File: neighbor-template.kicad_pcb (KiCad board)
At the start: 4 copper layers, 70.7 x 53.3 mm, 7 parts, among them J1 NEIGHBOR1, J2 NEIGHBOR2, J7 BONUS_ROW

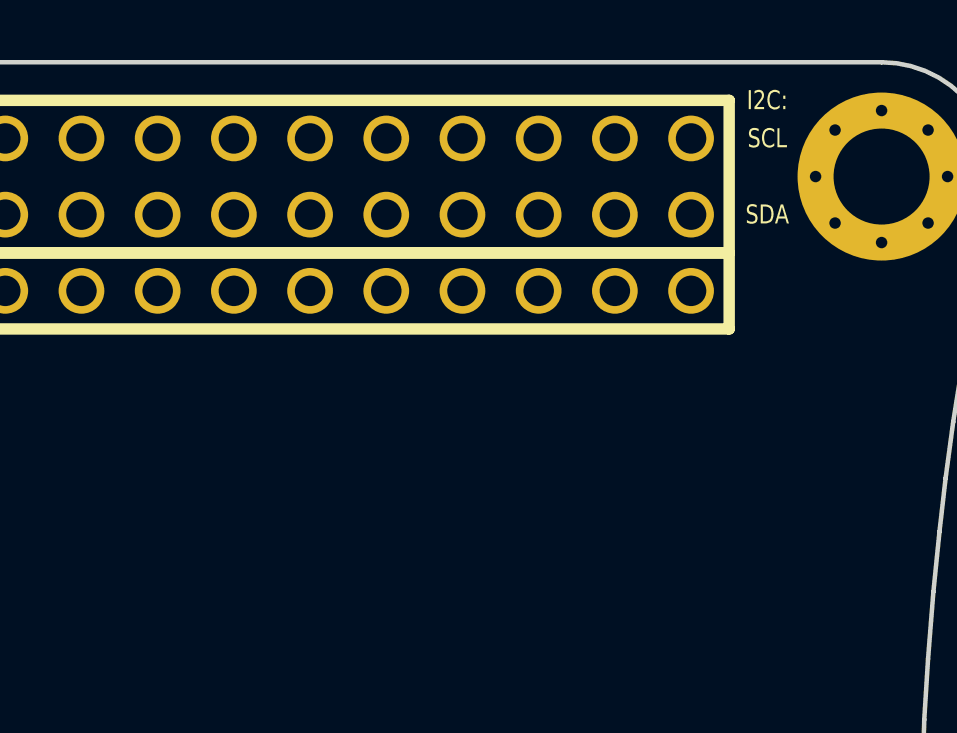
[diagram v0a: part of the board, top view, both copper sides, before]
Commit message: add identification EEPROM to layout
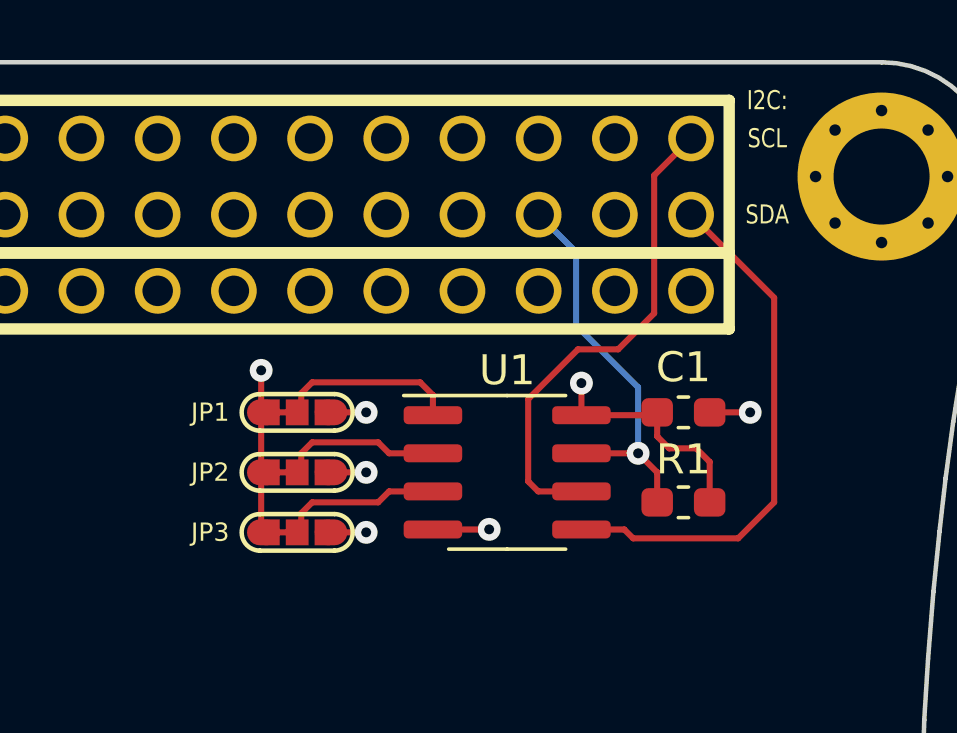
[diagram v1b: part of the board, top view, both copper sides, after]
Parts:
- added C1: 100nF, Capacitor_SMD:C_0603_1608Metric_Pad1.05x0.95mm_HandSolder, F.Cu at (169.9, 80.2)
- added JP1: Jumper_3_Bridged12, neighbor:0603-JUMPER-3-BRIDGED12, F.Cu at (157.1, 80.2)
- added JP2: Jumper_3_Bridged12, neighbor:0603-JUMPER-3-BRIDGED12, F.Cu at (157.1, 82.2)
- added JP3: Jumper_3_Bridged12, neighbor:0603-JUMPER-3-BRIDGED12, F.Cu at (157.1, 84.2)
- added R1: 10k, Resistor_SMD:R_0603_1608Metric_Pad1.05x0.95mm_HandSolder, F.Cu at (169.9, 83.2)
- added U1: M24C02-FMN6TP, Package_SO:SOIC-8_3.9x4.9mm_P1.27mm, F.Cu at (164.1, 82.2)
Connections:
- J1 pad 10: (no net) -> /P1_1
- J1 pad 11: (no net) -> /CLK0
- J1 pad 12: (no net) -> /P1_2
- J1 pad 13: (no net) -> /P1_5
- J1 pad 14: (no net) -> /P5_2
- J1 pad 15: (no net) -> /P1_7
- J1 pad 16: (no net) -> /P1_6
- J1 pad 17: (no net) -> /P1_9
- J1 pad 18: (no net) -> /P1_8
- J1 pad 19: (no net) -> /P5_3
- J1 pad 20: (no net) -> /P1_10
- J1 pad 21: (no net) -> /P1_12
- J1 pad 22: (no net) -> /P1_11
- J1 pad 23: (no net) -> /P5_5
- J1 pad 24: (no net) -> /P5_4
- J1 pad 25: (no net) -> /P1_14
- J1 pad 26: (no net) -> /P1_13
- J1 pad 27: (no net) -> /P5_6
- J1 pad 28: (no net) -> /P1_15
- J1 pad 29: (no net) -> /P5_7
- J1 pad 3: (no net) -> /P4_9
- J1 pad 30: (no net) -> /P1_16
- J1 pad 31: (no net) -> /P1_18
- J1 pad 32: (no net) -> /P1_17
- J1 pad 33: (no net) -> /P9_5
- J1 pad 34: (no net) -> /P9_6
- J1 pad 35: (no net) -> /P2_0
- J1 pad 36: (no net) -> /P6_0
- J1 pad 37: (no net) -> /P1_20
- J1 pad 38: (no net) -> /P1_19
- J1 pad 39: (no net) -> /P1_4
- J1 pad 4: (no net) -> /P0_0
- J1 pad 40: (no net) -> /P1_3
- J1 pad 5: (no net) -> /P4_10
- J1 pad 6: (no net) -> /P0_1
- J1 pad 7: (no net) -> /P1_0
- J1 pad 8: (no net) -> /P5_0
- J1 pad 9: (no net) -> /P5_1
- J2 pad 10: (no net) -> /P4_6
- J2 pad 11: (no net) -> /P4_7
- J2 pad 12: (no net) -> /CLK2
- J2 pad 13: (no net) -> /P2_8
- J2 pad 14: (no net) -> /P2_7
- J2 pad 15: (no net) -> /P2_6
- J2 pad 16: (no net) -> /P7_7
- J2 pad 17: (no net) -> /WAKEUP0
- J2 pad 18: (no net) -> /P2_5
- J2 pad 19: (no net) -> /P2_4
- J2 pad 20: (no net) -> /P2_3
- J2 pad 21: (no net) -> /PF_4
- J2 pad 22: (no net) -> /P3_2
- J2 pad 23: (no net) -> /P7_2
- J2 pad 24: (no net) -> /P3_1
- J2 pad 25: (no net) -> /P7_1
- J2 pad 26: (no net) -> /P3_0
- J2 pad 27: (no net) -> /P7_0
- J2 pad 28: (no net) -> /P3_4
- J2 pad 29: (no net) -> /P6_8
- J2 pad 3: (no net) -> /P4_8
- J2 pad 30: (no net) -> /P3_7
- J2 pad 31: (no net) -> /P6_7
- J2 pad 32: (no net) -> /P3_3
- J2 pad 33: (no net) -> /P2_2
- J2 pad 34: (no net) -> /P6_6
- J2 pad 35: (no net) -> /P2_1
- J2 pad 36: (no net) -> /P6_3
- J2 pad 37: (no net) -> /P3_5
- J2 pad 38: (no net) -> /P3_6
- J2 pad 39: (no net) -> /I2C0_SDA
- J2 pad 4: (no net) -> /P4_0
- J2 pad 40: (no net) -> /I2C0_SCL
- J2 pad 5: (no net) -> /ADC0_0
- J2 pad 6: (no net) -> /P4_5
- J2 pad 7: (no net) -> /P4_4
- J2 pad 8: (no net) -> /P4_2
- J2 pad 9: (no net) -> /P4_3
- J7 pad 11: (no net) -> /RESET
- J7 pad 12: (no net) -> /VBAT
- J7 pad 13: (no net) -> /P2_11
- J7 pad 14: (no net) -> /P2_10
- J7 pad 15: (no net) -> /P6_10
- J7 pad 16: (no net) -> /P6_9
- J7 pad 17: (no net) -> /P6_2
- J7 pad 18: (no net) -> /P6_1
- J7 pad 2: (no net) -> /P6_4
- J7 pad 3: (no net) -> /P6_5
- J7 pad 4: (no net) -> /ADC0_5
- J7 pad 5: (no net) -> /ADC0_2
- J7 pad 6: (no net) -> /P2_9
- J7 pad 7: (no net) -> /P2_12
- J7 pad 8: (no net) -> /P2_13
- J7 pad 9: (no net) -> /RTC_ALARM
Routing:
- net /I2C0_SDA: track 0.00 -> 17.8 mm
- net /I2C0_SCL: track 0.00 -> 16.4 mm
- net /P2_1: track 0.00 -> 13.1 mm, vias 0 -> 1
- net VCC: track 0.00 -> 11.4 mm, vias 0 -> 4
- net GND: track 0.00 -> 8.65 mm, vias 0 -> 3
- net /E0: track 0.00 -> 6.02 mm
- net /E2: track 0.00 -> 5.33 mm
- net /E1: track 0.00 -> 5.33 mm

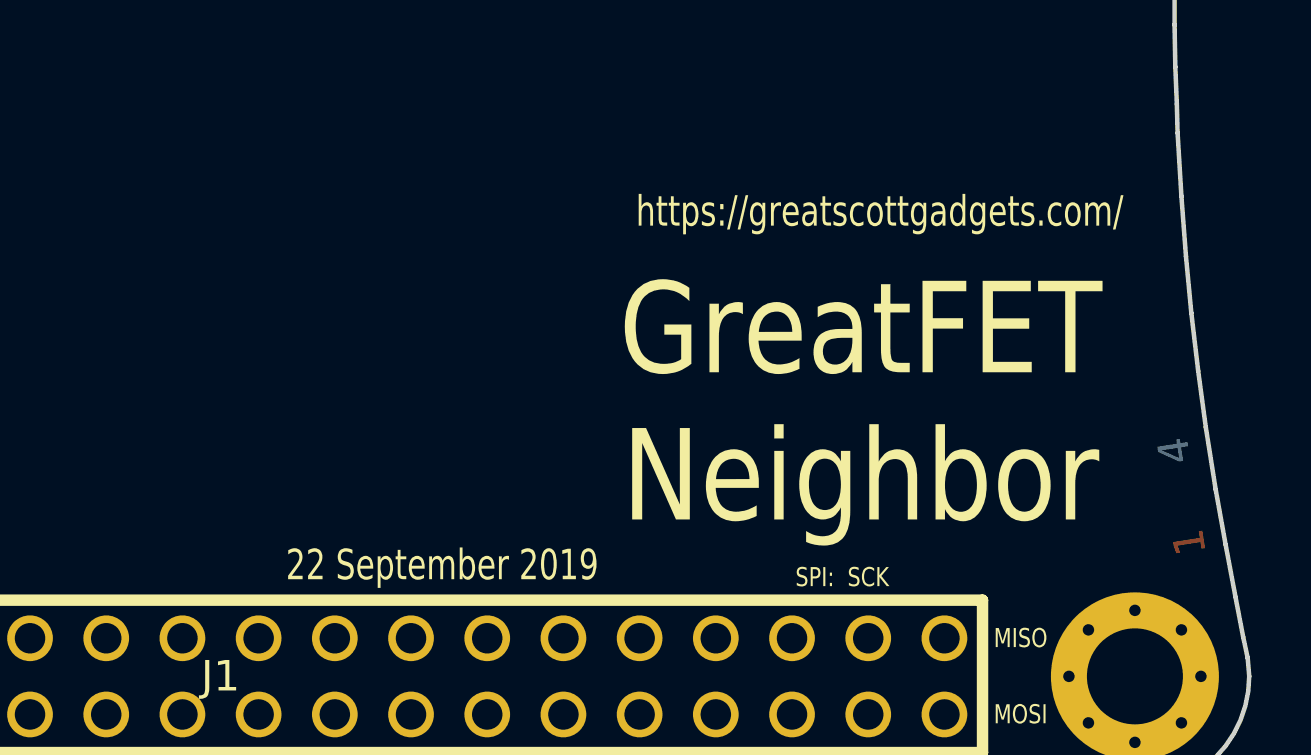
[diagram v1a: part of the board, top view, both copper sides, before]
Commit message: remove Great Scott Gadgets branding
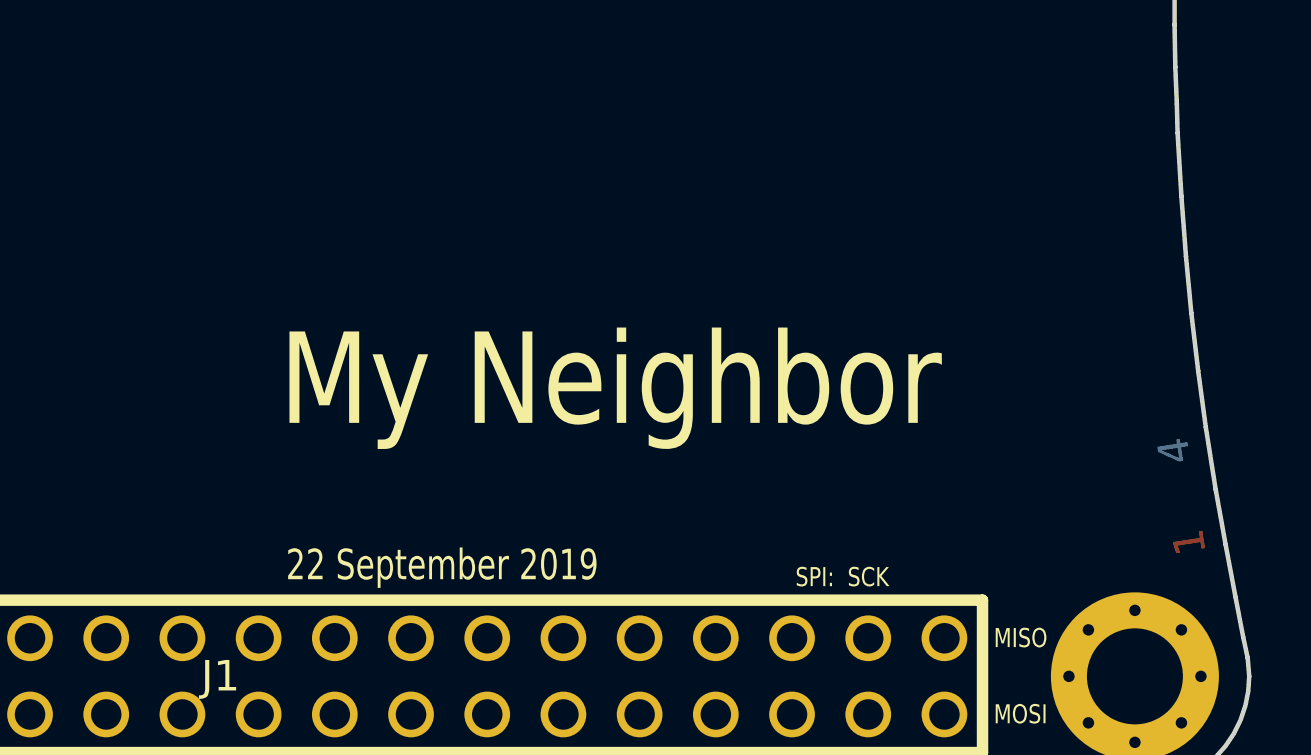
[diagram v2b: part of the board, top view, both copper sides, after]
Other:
- board text added: "My Neighbor"
- board text removed: "GreatFET Neighbor"
- board text removed: "https://greatscottgadgets.com/"
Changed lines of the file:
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@@
   (general
     (thickness 1.6)
-    (drawings 122)
+    (drawings 121)
     (tracks 64)
     (zones 0)
@@
     (effects (font (size 1.016 1.016) (thickness 0.1778)))
   )
-  (gr_text https://greatscottgadgets.com/ (at 168.021 102.616) (layer F.SilkS)
-    (effects (font (size 1.016 0.762) (thickness 0.1524)))
-  )
   (gr_text GND (at 118.999 73.406) (layer F.SilkS)
     (effects (font (size 0.635 0.508) (thickness 0.1016)))
@@
   (gr_arc (start 176.53 118.11) (end 180.34 118.11) (angle 90) (layer Edge.Cuts) (width 0.15))
   (gr_arc (start 279.4508 95.25) (end 177.8508 95.25) (angle 12.5) (layer Cmts.User) (width 0.15))
-  (gr_text "GreatFET\nNeighbor" (at 167.386 109.0168) (layer F.SilkS)
+  (gr_text "My Neighbor" (at 159.05 108.25) (layer F.SilkS)
     (effects (font (size 3.048 2.54) (thickness 0.4572)))
   )
@@
   (segment (start 168.95 76.95) (end 167.75 78.15) (width 0.2032) (layer F.Cu) (net 79))
   (segment (start 166.410198 78.15) (end 164.75 79.810198) (width 0.2032) (layer F.Cu) (net 79))
+  (segment (start 161.575 80.345) (end 161.575 79.675) (width 0.2032) (layer F.Cu) (net 96))
+  (segment (start 161.575 79.675) (end 161.15 79.25) (width 0.2032) (layer F.Cu) (net 96))
+  (segment (start 161.15 79.25) (end 157.55 79.25) (width 0.2032) (layer F.Cu) (net 96))
+  (segment (start 157.185001 79.945199) (end 157.185001 80.25) (width 0.2032) (layer F.Cu) (net 96))
+  (segment (start 157.55 79.25) (end 157.185001 79.614999) (width 0.2032) (layer F.Cu) (net 96))
+  (segment (start 157.185001 79.614999) (end 157.185001 79.945199) (width 0.2032) (layer F.Cu) (net 96))
+  (segment (start 161.575 81.615) (end 160.115 81.615) (width 0.2032) (layer F.Cu) (net 97))
+  (segment (start 160.115 81.615) (end 159.75 81.25) (width 0.2032) (layer F.Cu) (net 97))
+  (segment (start 159.75 81.25) (end 157.55 81.25) (width 0.2032) (layer F.Cu) (net 97))
+  (segment (start 157.185001 81.945199) (end 157.185001 82.25) (width 0.2032) (layer F.Cu) (net 97))
+  (segment (start 157.55 81.25) (end 157.185001 81.614999) (width 0.2032) (layer F.Cu) (net 97))
+  (segment (start 157.185001 81.614999) (end 157.185001 81.945199) (width 0.2032) (layer F.Cu) (net 97))
   (segment (start 161.575 82.885) (end 160.115 82.885) (width 0.2032) (layer F.Cu) (net 98))
   (segment (start 160.115 82.885) (end 159.75 83.25) (width 0.2032) (layer F.Cu) (net 98))
@@
   (segment (start 157.55 83.25) (end 157.185001 83.614999) (width 0.2032) (layer F.Cu) (net 98))
   (segment (start 157.185001 83.614999) (end 157.185001 83.945199) (width 0.2032) (layer F.Cu) (net 98))
-  (segment (start 161.575 81.615) (end 160.115 81.615) (width 0.2032) (layer F.Cu) (net 97))
-  (segment (start 160.115 81.615) (end 159.75 81.25) (width 0.2032) (layer F.Cu) (net 97))
-  (segment (start 159.75 81.25) (end 157.55 81.25) (width 0.2032) (layer F.Cu) (net 97))
-  (segment (start 157.185001 81.945199) (end 157.185001 82.25) (width 0.2032) (layer F.Cu) (net 97))
-  (segment (start 157.55 81.25) (end 157.185001 81.614999) (width 0.2032) (layer F.Cu) (net 97))
-  (segment (start 157.185001 81.614999) (end 157.185001 81.945199) (width 0.2032) (layer F.Cu) (net 97))
-  (segment (start 161.575 80.345) (end 161.575 79.675) (width 0.2032) (layer F.Cu) (net 96))
-  (segment (start 161.575 79.675) (end 161.15 79.25) (width 0.2032) (layer F.Cu) (net 96))
-  (segment (start 161.15 79.25) (end 157.55 79.25) (width 0.2032) (layer F.Cu) (net 96))
-  (segment (start 157.185001 79.945199) (end 157.185001 80.25) (width 0.2032) (layer F.Cu) (net 96))
-  (segment (start 157.55 79.25) (end 157.185001 79.614999) (width 0.2032) (layer F.Cu) (net 96))
-  (segment (start 157.185001 79.614999) (end 157.185001 79.945199) (width 0.2032) (layer F.Cu) (net 96))
   (zone (net 2) (net_name VCC) (layer C3.Cu) (hatch edge 0.508)
     (connect_pads (clearance 0.254))

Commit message: change J7_P10 from GND to RTCX1 fixes #7
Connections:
- J7 pad 10: GND -> /RTCX1
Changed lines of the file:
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@@
     (zones 0)
     (modules 13)
-    (nets 99)
+    (nets 100)
   )
   (page A4)
@@
   (net 97 /E1)
   (net 98 /E2)
+  (net 99 /RTCX1)
   (net_class Default "This is the default net class."
     (clearance 0.1524)
@@
     (add_net /PF_4)
     (add_net /RESET)
+    (add_net /RTCX1)
     (add_net /RTC_ALARM)
     (add_net /VBAT)
@@
       (net 87 /RTC_ALARM))
     (pad 10 thru_hole circle (at -1.27 0) (size 1.524 1.524) (drill 1.016) (layers *.Cu *.Mask F.SilkS)
-      (net 1 GND))
+      (net 99 /RTCX1))
     (pad 11 thru_hole circle (at 1.27 0) (size 1.524 1.524) (drill 1.016) (layers *.Cu *.Mask F.SilkS)
       (net 88 /RESET))

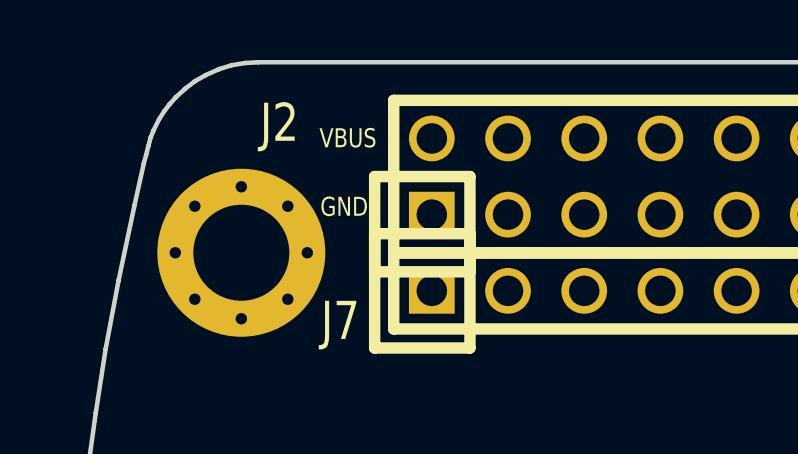
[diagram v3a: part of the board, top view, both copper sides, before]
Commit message: change J2_P2 from VBUS to +5V fixes #8
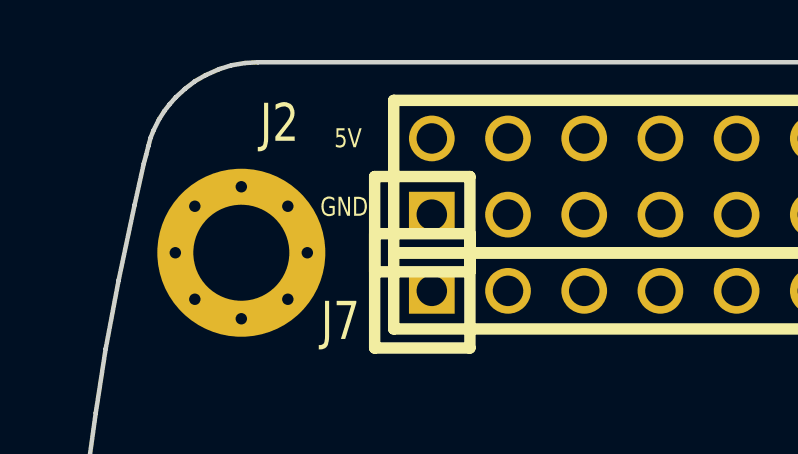
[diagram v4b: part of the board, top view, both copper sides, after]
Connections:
- net /VBUS renamed +5V
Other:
- board text added: "5V"
- board text removed: "VBUS"

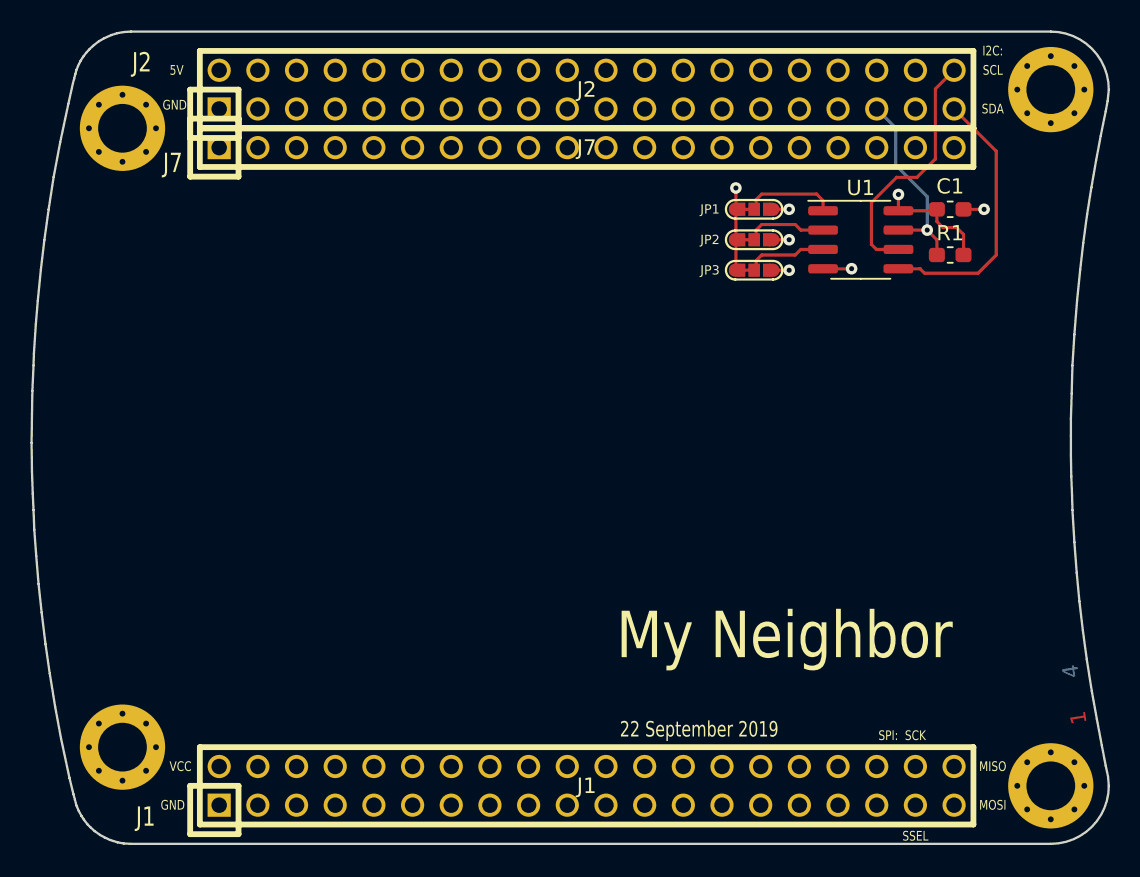
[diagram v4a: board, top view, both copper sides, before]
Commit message: add pin numbers to silkscreen update silkscreen to match Azalea closes #5
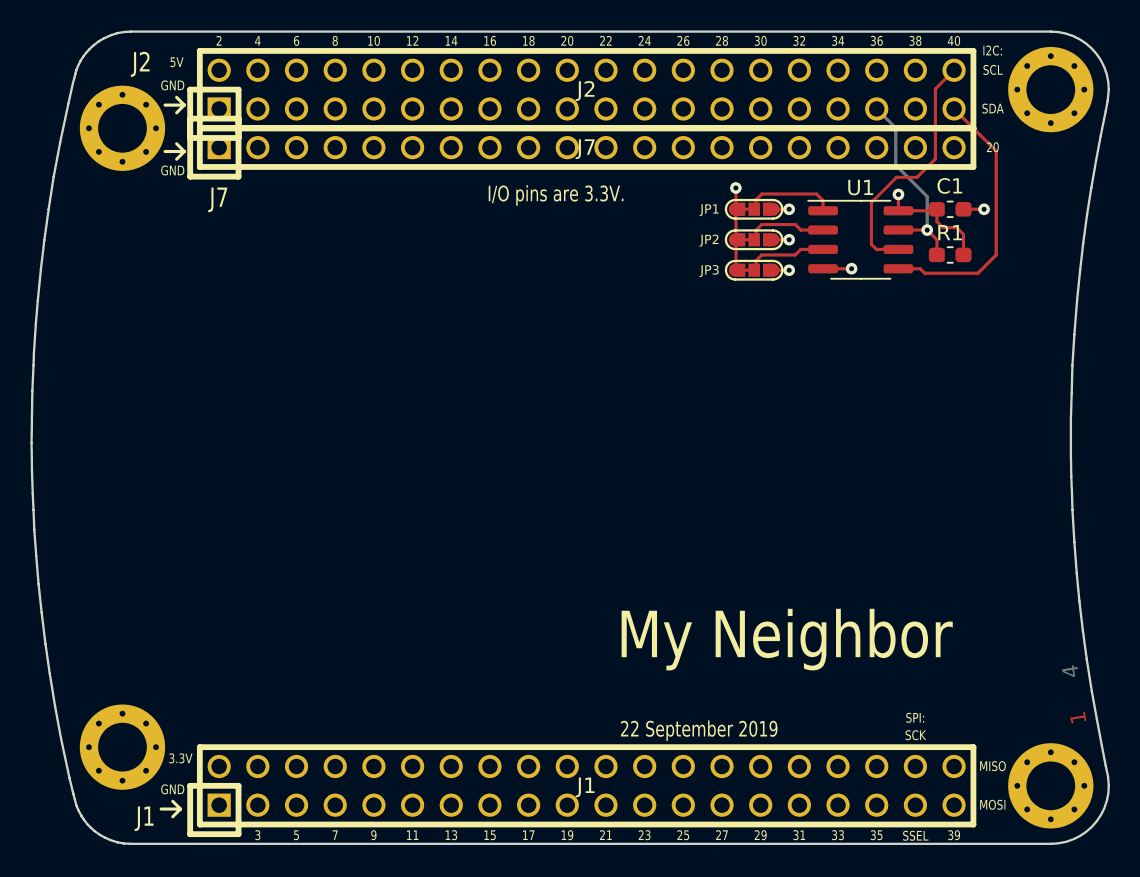
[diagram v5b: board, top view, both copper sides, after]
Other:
- board text added: "10"
- board text added: "11"
- board text added: "12"
- board text added: "13"
- board text added: "14"
- board text added: "15"
- board text added: "16"
- board text added: "17"
- board text added: "18"
- board text added: "19"
- board text added: "20"
- board text added: "21"
- board text added: "22"
- board text added: "23"
- board text added: "24"
- board text added: "25"
- board text added: "26"
- board text added: "27"
- board text added: "28"
- board text added: "29"
- board text added: "3.3V"
- board text added: "30"
- board text added: "31"
- board text added: "32"
- board text added: "33"
- board text added: "34"
- board text added: "35"
- board text added: "36"
- board text added: "38"
- board text added: "39"
- board text added: "40"
- board text added: "5"
- board text added: "6"
- board text added: "7"
- board text added: "8"
- board text added: "9"
- board text added: "I/O pins are 3.3V."
- board text removed: "VCC"
